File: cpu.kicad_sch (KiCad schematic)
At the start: 32 parts, among them IC101 HUC6280, IC106 UPC358

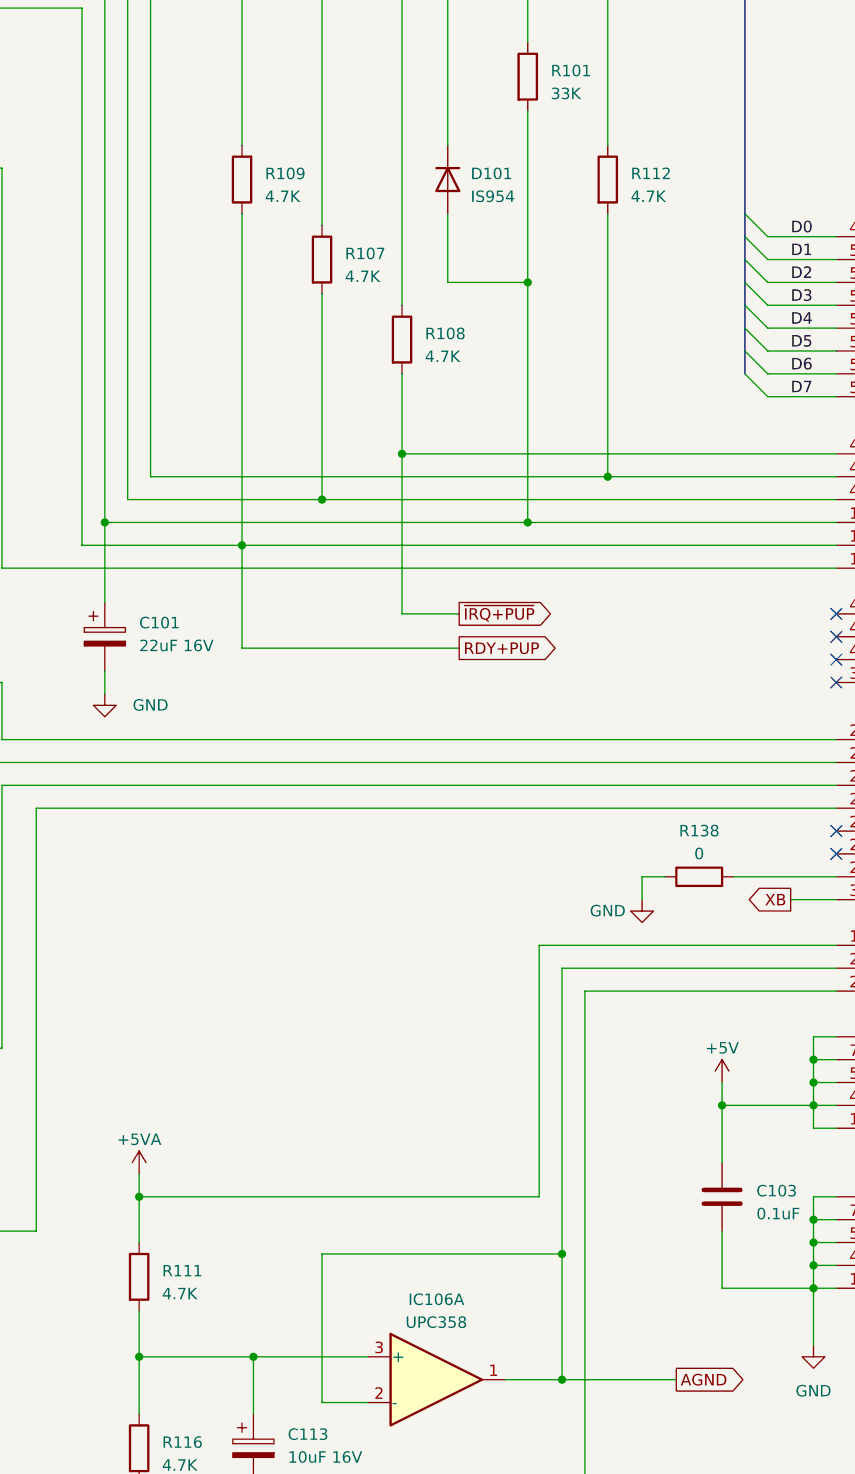
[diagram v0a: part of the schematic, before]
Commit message: Add SMD 1206 footprint and some passives.
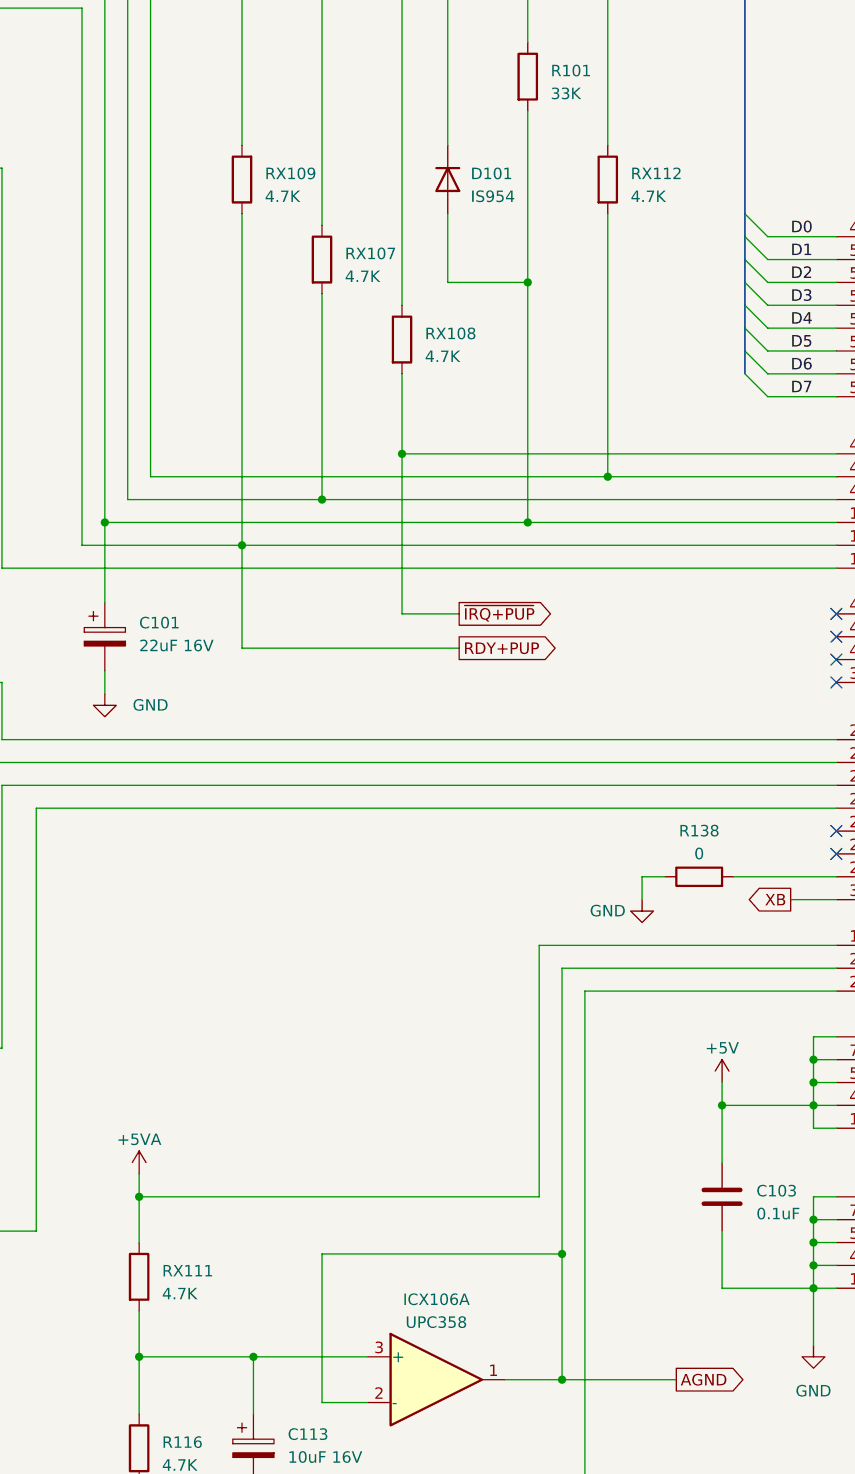
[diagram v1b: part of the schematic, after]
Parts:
- renumbered IC106 to ICX106, R107 to RX107, R108 to RX108, R109 to RX109, R111 to RX111, R112 to RX112
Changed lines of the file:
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@@
   (symbol (lib_id "Device:R") (at 135.89 73.66 0) (unit 1)
     (in_bom yes) (on_board yes) (dnp no) (fields_autoplaced)
-    (property "Reference" "R107" (at 138.43 73.025 0)
+    (property "Reference" "RX107" (at 138.43 73.025 0)
       (effects (font (size 1.27 1.27)) (justify left))
     )
@@
       (project "PCE"
         (path "/c1c718c6-a427-431e-a18b-e46f94ae8e09/1d91d06a-381a-4a70-bfc1-2abf4d159a91"
-          (reference "R107") (unit 1)
+          (reference "RX107") (unit 1)
         )
       )
@@
   (symbol (lib_id "Device:R") (at 167.64 64.77 0) (unit 1)
     (in_bom yes) (on_board yes) (dnp no) (fields_autoplaced)
-    (property "Reference" "R112" (at 170.18 64.135 0)
+    (property "Reference" "RX112" (at 170.18 64.135 0)
       (effects (font (size 1.27 1.27)) (justify left))
     )
@@
       (project "PCE"
         (path "/c1c718c6-a427-431e-a18b-e46f94ae8e09/1d91d06a-381a-4a70-bfc1-2abf4d159a91"
-          (reference "R112") (unit 1)
+          (reference "RX112") (unit 1)
         )
       )
@@
   (symbol (lib_id "Device:R") (at 127 64.77 180) (unit 1)
     (in_bom yes) (on_board yes) (dnp no) (fields_autoplaced)
-    (property "Reference" "R109" (at 129.54 64.135 0)
+    (property "Reference" "RX109" (at 129.54 64.135 0)
       (effects (font (size 1.27 1.27)) (justify right))
     )
@@
       (project "PCE"
         (path "/c1c718c6-a427-431e-a18b-e46f94ae8e09/1d91d06a-381a-4a70-bfc1-2abf4d159a91"
-          (reference "R109") (unit 1)
+          (reference "RX109") (unit 1)
         )
       )
@@
   (symbol (lib_id "Device:R") (at 144.78 82.55 0) (unit 1)
     (in_bom yes) (on_board yes) (dnp no) (fields_autoplaced)
-    (property "Reference" "R108" (at 147.32 81.915 0)
+    (property "Reference" "RX108" (at 147.32 81.915 0)
       (effects (font (size 1.27 1.27)) (justify left))
     )
@@
       (project "PCE"
         (path "/c1c718c6-a427-431e-a18b-e46f94ae8e09/1d91d06a-381a-4a70-bfc1-2abf4d159a91"
-          (reference "R108") (unit 1)
+          (reference "RX108") (unit 1)
         )
       )
@@
   (symbol (lib_id "Amplifier_Operational:LM358") (at 148.59 198.12 0) (unit 1)
     (in_bom yes) (on_board yes) (dnp no) (fields_autoplaced)
-    (property "Reference" "IC106" (at 148.59 189.23 0)
+    (property "Reference" "ICX106" (at 148.59 189.23 0)
       (effects (font (size 1.27 1.27)))
     )
@@
       (project "PCE"
         (path "/c1c718c6-a427-431e-a18b-e46f94ae8e09/1d91d06a-381a-4a70-bfc1-2abf4d159a91"
-          (reference "IC106") (unit 1)
+          (reference "ICX106") (unit 1)
         )
       )
@@
   (symbol (lib_id "Device:R") (at 115.57 186.69 0) (unit 1)
     (in_bom yes) (on_board yes) (dnp no) (fields_autoplaced)
-    (property "Reference" "R111" (at 118.11 186.055 0)
+    (property "Reference" "RX111" (at 118.11 186.055 0)
       (effects (font (size 1.27 1.27)) (justify left))
     )
@@
       (project "PCE"
         (path "/c1c718c6-a427-431e-a18b-e46f94ae8e09/1d91d06a-381a-4a70-bfc1-2abf4d159a91"
-          (reference "R111") (unit 1)
-        )
-      )
+          (reference "RX111") (unit 1)
+        )
+      )

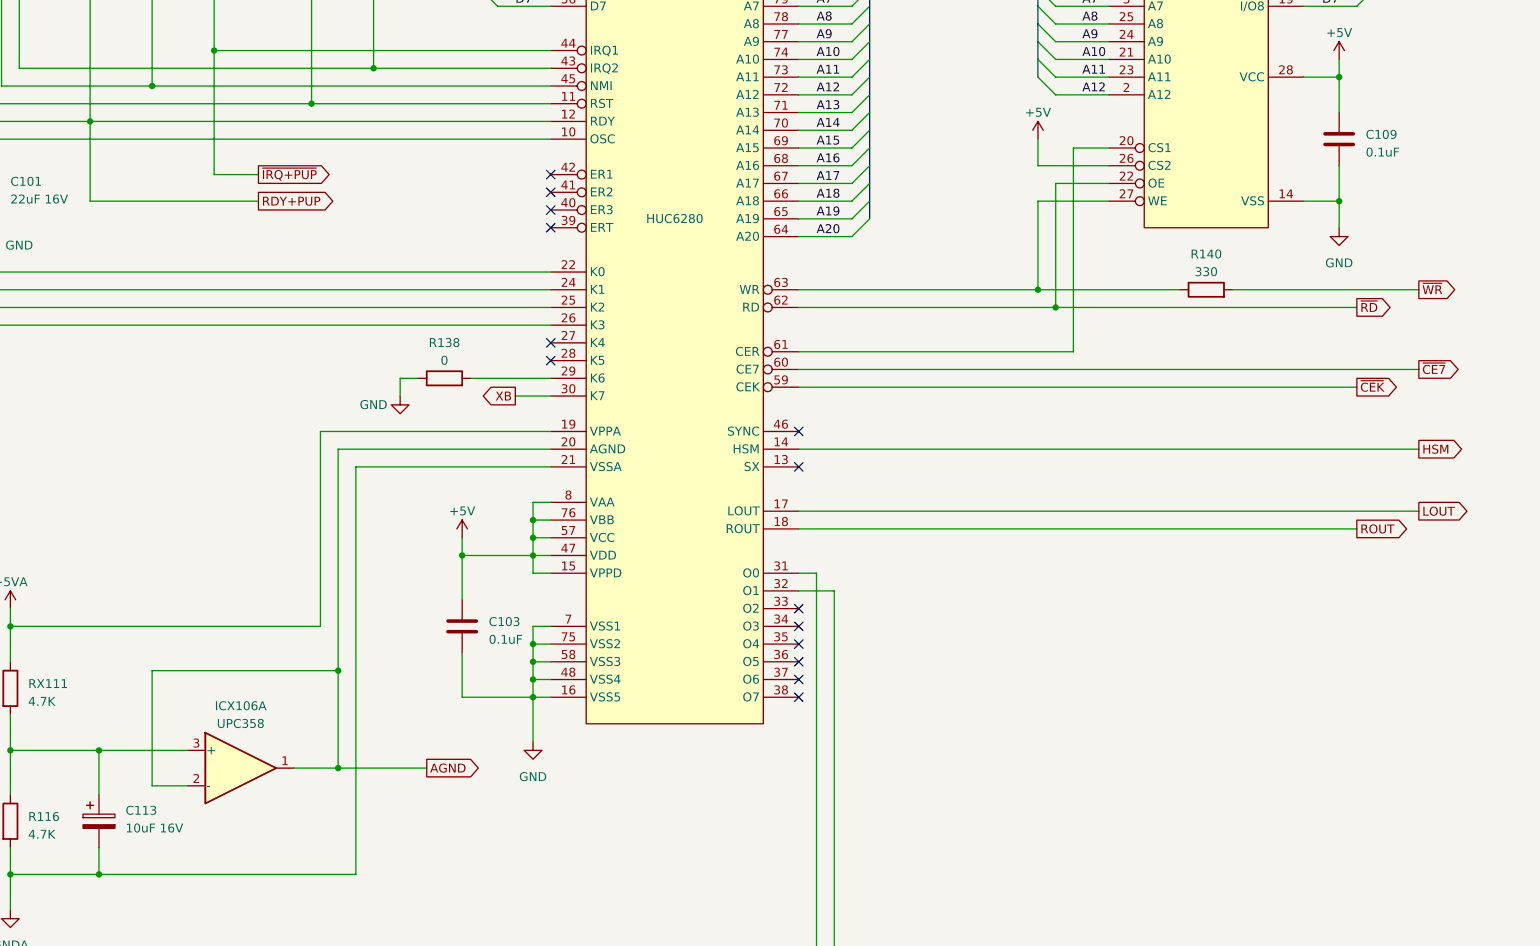
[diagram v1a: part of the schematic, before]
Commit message: Work out numbering of and route some caps.
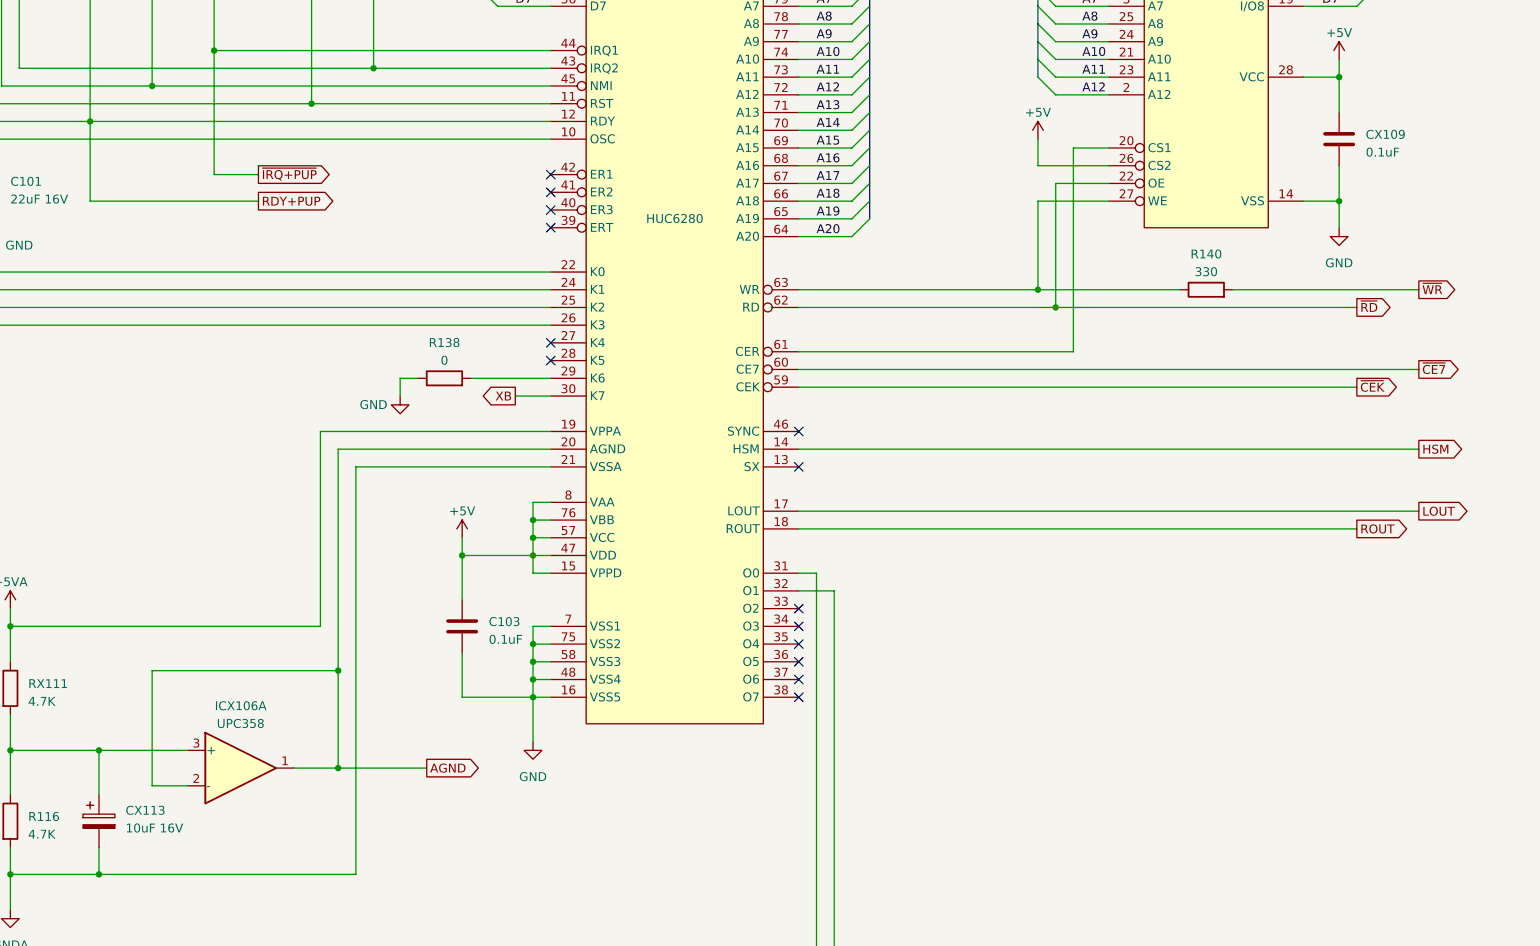
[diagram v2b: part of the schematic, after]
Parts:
- C101: footprint (none) -> A-PCENGINE:Elec_P5.00mm
- CX113: renamed from C113; footprint (none) -> A-PCENGINE:Elec_P5.00mm
- renumbered C109 to CX109
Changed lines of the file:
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@@
   (symbol (lib_id "Device:C_Polarized") (at 128.27 205.74 0) (unit 1)
     (in_bom yes) (on_board yes) (dnp no) (fields_autoplaced)
-    (property "Reference" "C113" (at 132.08 204.216 0)
+    (property "Reference" "CX113" (at 132.08 204.216 0)
       (effects (font (size 1.27 1.27)) (justify left))
     )
@@
       (effects (font (size 1.27 1.27)) (justify left))
     )
-    (property "Footprint" "" (at 129.2352 209.55 0)
+    (property "Footprint" "A-PCENGINE:Elec_P5.00mm" (at 129.2352 209.55 0)
       (effects (font (size 1.27 1.27)) hide)
     )
@@
       (project "PCE"
         (path "/c1c718c6-a427-431e-a18b-e46f94ae8e09/1d91d06a-381a-4a70-bfc1-2abf4d159a91"
-          (reference "C113") (unit 1)
+          (reference "CX113") (unit 1)
         )
       )
@@
       (effects (font (size 1.27 1.27)) (justify left))
     )
-    (property "Footprint" "" (at 112.7252 119.38 0)
+    (property "Footprint" "A-PCENGINE:Elec_P5.00mm" (at 112.7252 119.38 0)
       (effects (font (size 1.27 1.27)) hide)
     )
@@
   (symbol (lib_id "Device:C") (at 306.07 107.95 0) (unit 1)
     (in_bom yes) (on_board yes) (dnp no) (fields_autoplaced)
-    (property "Reference" "C109" (at 309.88 107.315 0)
+    (property "Reference" "CX109" (at 309.88 107.315 0)
       (effects (font (size 1.27 1.27)) (justify left))
     )
@@
       (project "PCE"
         (path "/c1c718c6-a427-431e-a18b-e46f94ae8e09/1d91d06a-381a-4a70-bfc1-2abf4d159a91"
-          (reference "C109") (unit 1)
-        )
-      )
+          (reference "CX109") (unit 1)
+        )
+      )

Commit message: Intermediate save
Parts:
- removed R140: 330, symbol Device:R
- added R155: 4.7K, A-PCENGINE:SMD_1206, symbol Device:R
- C104, C105, C106, CX109: footprint (none) -> A-PCENGINE:SMD_1206_C
- C138: renamed from C107; footprint (none) -> A-PCENGINE:SMD_1206_C
- CY102: renamed from C102; footprint (none) -> A-PCENGINE:SMD_1206_C
- CY103: renamed from C103; footprint (none) -> A-PCENGINE:SMD_1206_C
- FL101, FL102, FL103, FL104, FL105, FL106, FL107: footprint (none) -> A-PCENGINE:FL-5.00mm
- R103: renamed from RX112; footprint (none) -> A-PCENGINE:SMD_1206
- R117: renamed from R103; footprint (none) -> A-PCENGINE:SMD_1206
- R118: renamed from R102; footprint (none) -> A-PCENGINE:SMD_1206
- R163: renamed from R104; footprint (none) -> A-PCENGINE:SMD_1206
- renumbered R101 to RX101, R116 to RX116
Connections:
- net +5V: now also FL101.3, R117.2, R155.1; no longer FL106.3, R118.2
- net CLR: now also FL107.1; no longer FL103.1
- net DI1: now also FL103.1; no longer FL107.1
- net DI3: now also FL105.1; no longer FL101.1
- net GND: now also R118.2; no longer R117.2
- net SEL: now also FL106.1; no longer FL105.1
- net VDD: now also FL101.1; no longer FL106.1
- net ~{CEK}: now also R155.2
- net ~{WR}: now also IC101.63 (WR), ICX102.27 (WE)
- net at IC101.26 (K3): now also FL105.3; no longer FL101.3
- net at FL103.3: now also IC101.24 (K1); no longer IC101.32 (O1)
- net at FL107.3: now also IC101.32 (O1); no longer IC101.24 (K1)
- net at IC101.31 (O0): now also FL106.3; no longer FL105.3
- net ~{CER}: now reaches IC101.61 (CER), ICX102.20 (CS1)
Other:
- moved on the sheet: FL101, FL103, FL105, FL106, FL107, R117, R118
